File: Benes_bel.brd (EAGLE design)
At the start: 91.1 x 58.4 mm, 19 parts, among them J1 DCJ0202, K1 HE751, K2 HE751, K3 HE751, K4 HE751, T1 BC337, T2 BC337, T3 BC337, T4 BC337, X5 FH12-08S-1SH

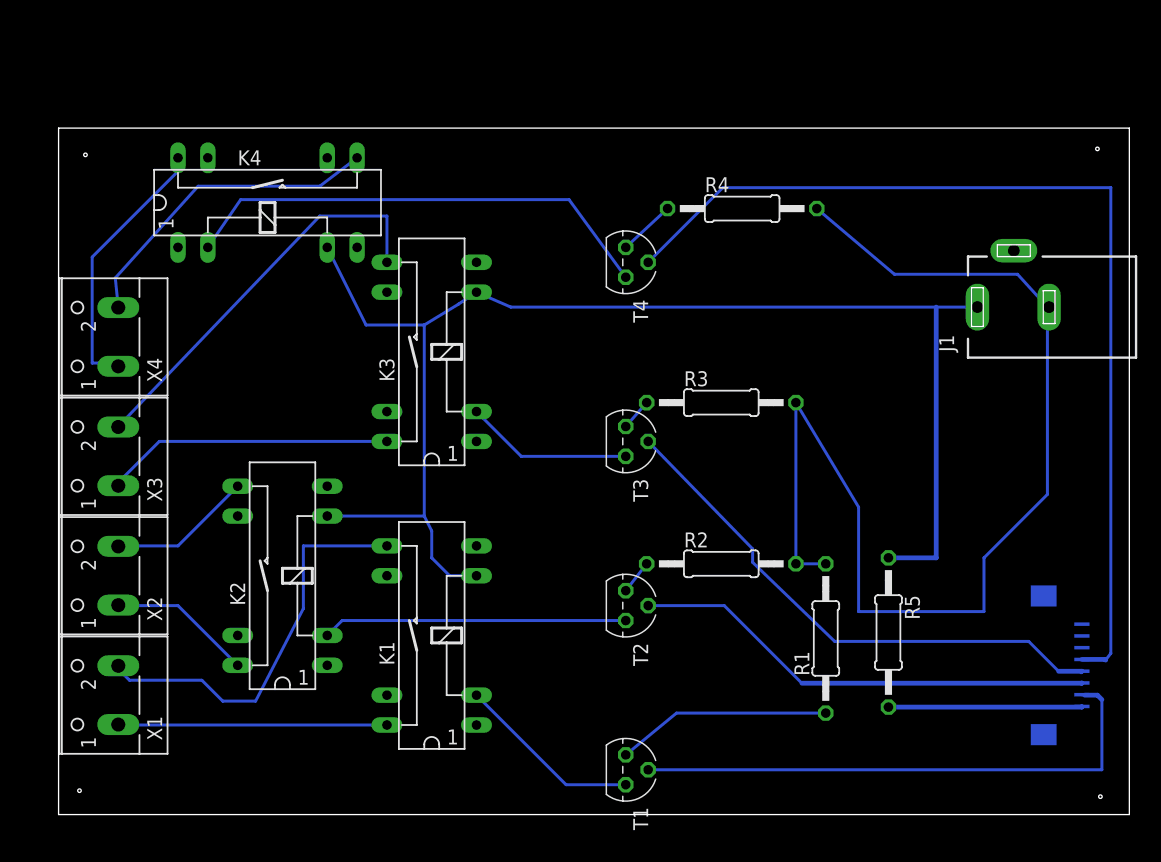
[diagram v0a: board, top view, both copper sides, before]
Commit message: Aanpassing van Benes_bel
dikkere lijnen, groter afstand voor frezen
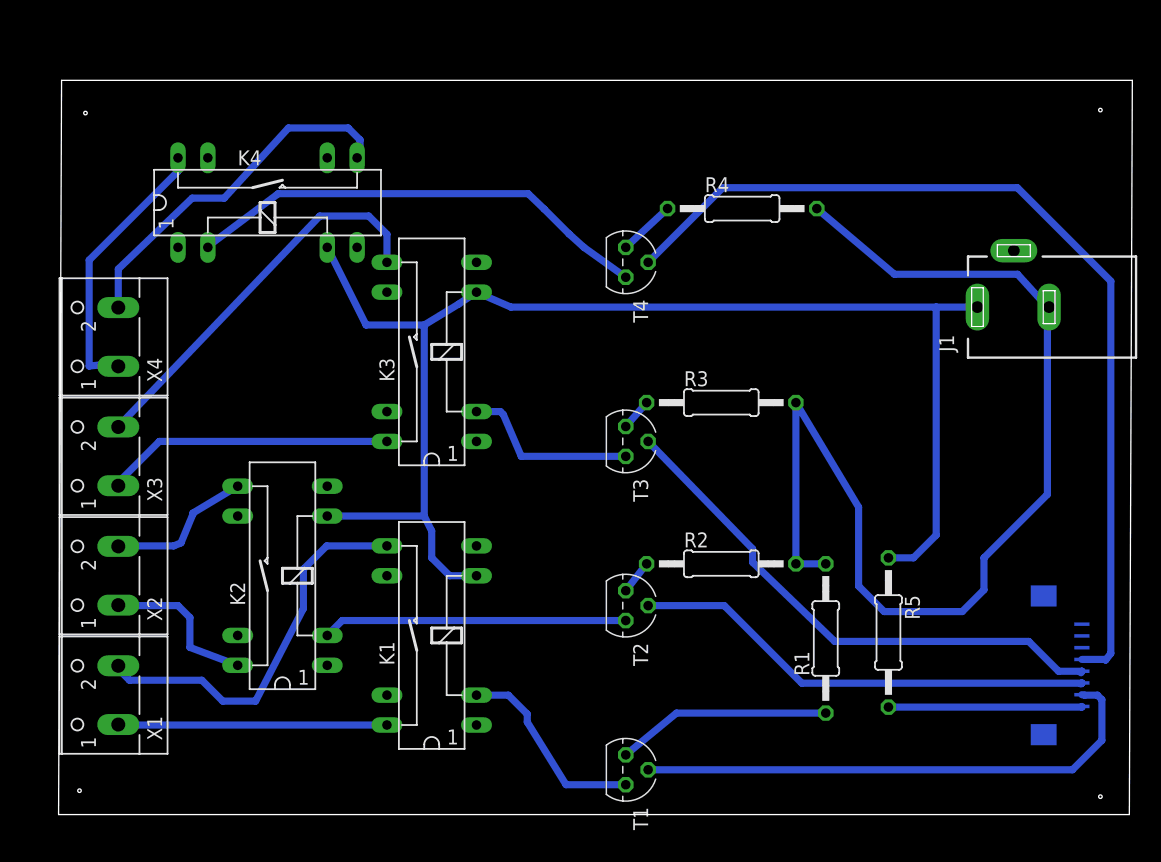
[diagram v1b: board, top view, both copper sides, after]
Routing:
- net N$10: track 84.4 -> 79.8 mm
- net N$18: track 27.4 -> 31.0 mm
- net N$6: track 97.4 -> 95.0 mm
- net N$7: track 46.4 -> 45.0 mm
- net N$20: track 41.1 -> 39.8 mm
- net N$12: track 34.4 -> 33.2 mm
- net N$23: track 15.9 -> 17.0 mm
- net N$21: track 118.5 -> 117.4 mm
- net N$13: track 12.3 -> 13.4 mm
- net N$16: track 34.5 -> 33.6 mm
- net N$19: track 14.3 -> 15.2 mm
- net N$17: track 23.0 -> 23.6 mm
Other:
- board size 91.1 x 58.4 mm -> 91.4 x 62.5 mm

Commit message: aanpassing met extra leds als controle tracks op 2 lagen Gerber files
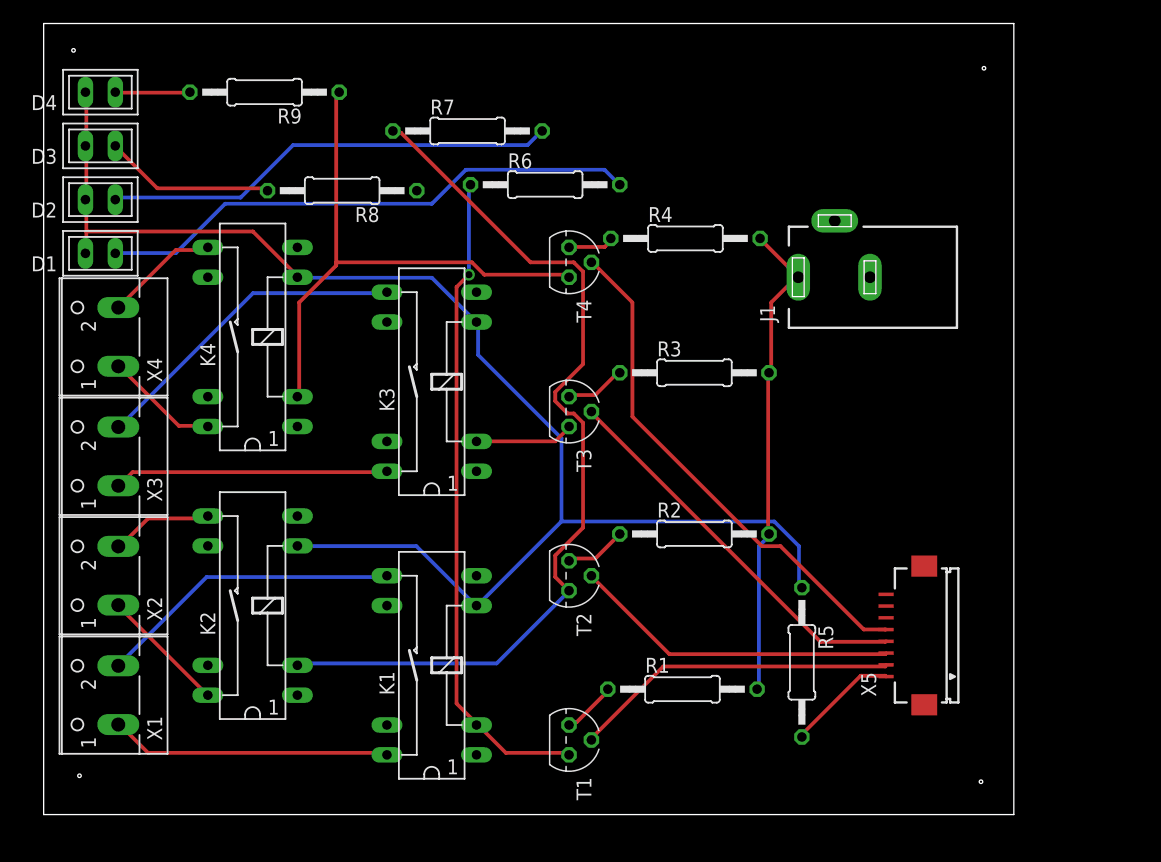
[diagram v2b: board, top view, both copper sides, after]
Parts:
- added D1, D2, D3, D4: U57X32, led:U57X32
- added R6, R7, R8, R9: 330k, resistor:0207/12
- moved J1 15.5 mm to (66.0, 45.7)
- moved R1 12.9 mm to (53.1, 10.7), turned to 0 degrees
- moved K4 11.5 mm to (16.5, 40.6), turned to 90 degrees
- moved X5 10.5 mm to (73.7, 15.2), flipped to the top
- moved R5 7.79 mm to (63.2, 13.0)
- moved T1 5.45 mm to (43.4, 6.35)
- moved T2 5.45 mm to (43.4, 20.3)
- moved T3 5.45 mm to (43.4, 34.3)
- moved R4 5.45 mm to (53.3, 49.0)
- moved T4 4.83 mm to (43.4, 47.0)
- moved K2 3.59 mm to (16.5, 17.8)
- moved R2 3.42 mm to (54.1, 23.9)
- moved R3 3.42 mm to (54.1, 37.6)
- moved K1 2.54 mm to (31.8, 12.7)
- moved K3 2.54 mm to (31.8, 36.8)
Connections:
- removed net N$21: J1.1, K1.6, K2.6, K3.6, K4.6, R5.1
- new net N$24: D4.A, R9.2
- new net N$25: D1.A, R6.2
- new net N$26: D2.A, R7.2
- new net N$27: D3.A, R8.2
- new net N$28: D1.K, D2.K, D3.K, D4.K, K1.6, K2.6, K3.6, K4.6, R5.1
- new net N$30: R8.1
- net N$20: now also R9.1
- net N$23: now also R6.1
- net N$5: now also R7.1
- net N$6: now also J1.1; no longer J1.3
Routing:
- net N$28: track 0.00 -> 122.6 mm
- net N$21: track 117.4 -> 0.00 mm
- net N$6: track 95.0 -> 41.3 mm
- net N$5: track 25.9 -> 77.8 mm
- net N$25: track 0.00 -> 46.4 mm
- net N$23: track 17.0 -> 56.1 mm, vias 0 -> 1
- net N$26: track 0.00 -> 38.7 mm
- net N$10: track 79.8 -> 43.7 mm
- net N$18: track 31.0 -> 9.79 mm
- net N$7: track 45.0 -> 27.8 mm
- net N$27: track 0.00 -> 14.5 mm
- net N$17: track 23.6 -> 9.72 mm
- net N$1: track 18.3 -> 4.70 mm
- net N$9: track 45.8 -> 33.2 mm
- net N$8: track 39.8 -> 27.9 mm
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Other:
- board size 91.4 x 62.5 mm -> 82.5 x 67.3 mm

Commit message: Bord werkt op eerste pcb ontbreken 3 draden in de schema's en de prod files is dit aangepast.
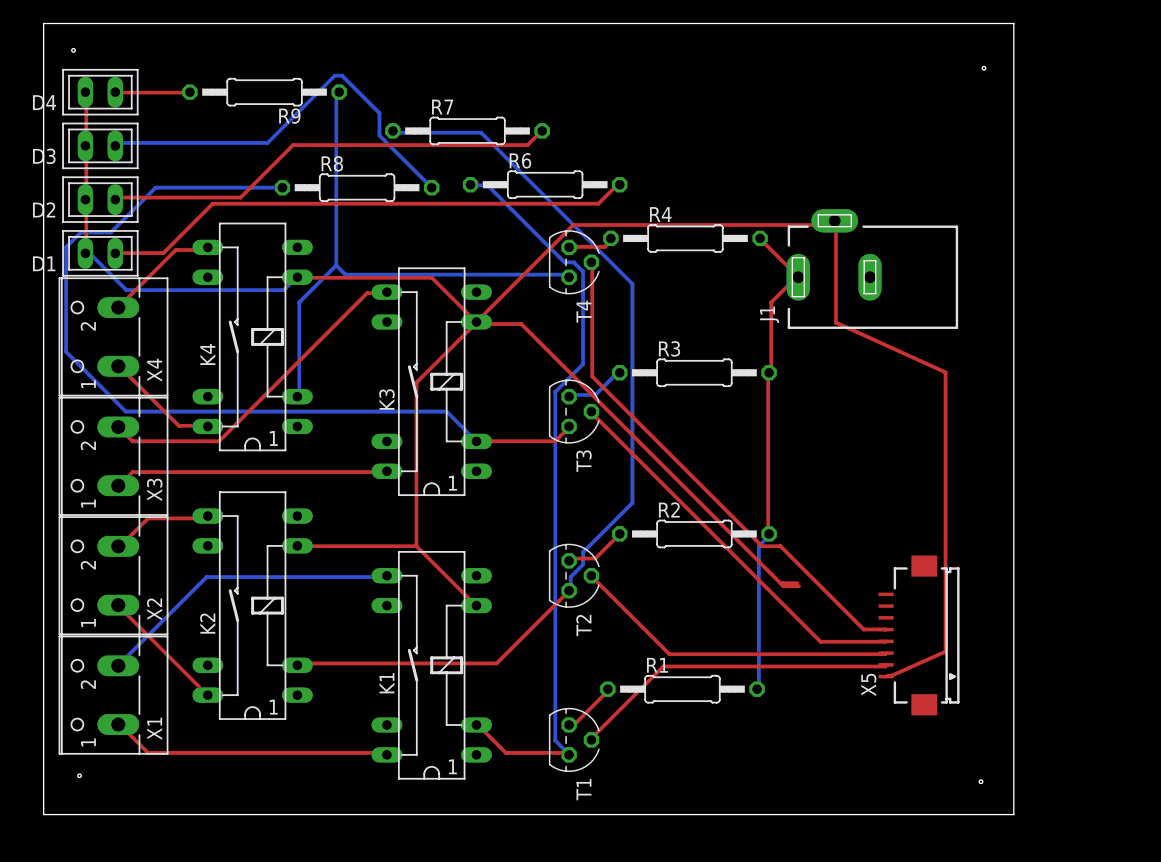
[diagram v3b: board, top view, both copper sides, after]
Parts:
- removed R5: (no value), resistor:0207/12
- moved R8 1.30 mm to (25.4, 53.3), turned to 0 degrees
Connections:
- removed net N$22: R5.2, X5.1
- removed net N$28: D1.K, D2.K, D3.K, D4.K, K1.6, K2.6, K3.6, K4.6, R5.1
- removed net N$30: R8.1
- new net N$21: D1.K, D2.K, D3.K, D4.K, J1.2, K1.6, K2.6, K3.6, K4.6, X5.1
- net N$19: now also R8.1
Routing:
- net N$21: track 0.00 -> 209.6 mm
- net N$28: track 122.6 -> 0.00 mm
- net N$19: track 8.43 -> 75.9 mm
- net N$27: track 14.5 -> 34.5 mm
- net N$22: track 9.47 -> 0.00 mm
- net N$23: track 56.1 -> 64.1 mm, vias 1 -> 0
- net N$5: track 77.8 -> 79.9 mm
- net N$25: track 46.4 -> 45.3 mm
- net N$16: track 27.6 -> 28.6 mm
- net N$6: track 41.3 -> 42.0 mm

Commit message: correctie bord: groter gaten vr DC Jack toevoeging van vcc naar display leds meer ruimte
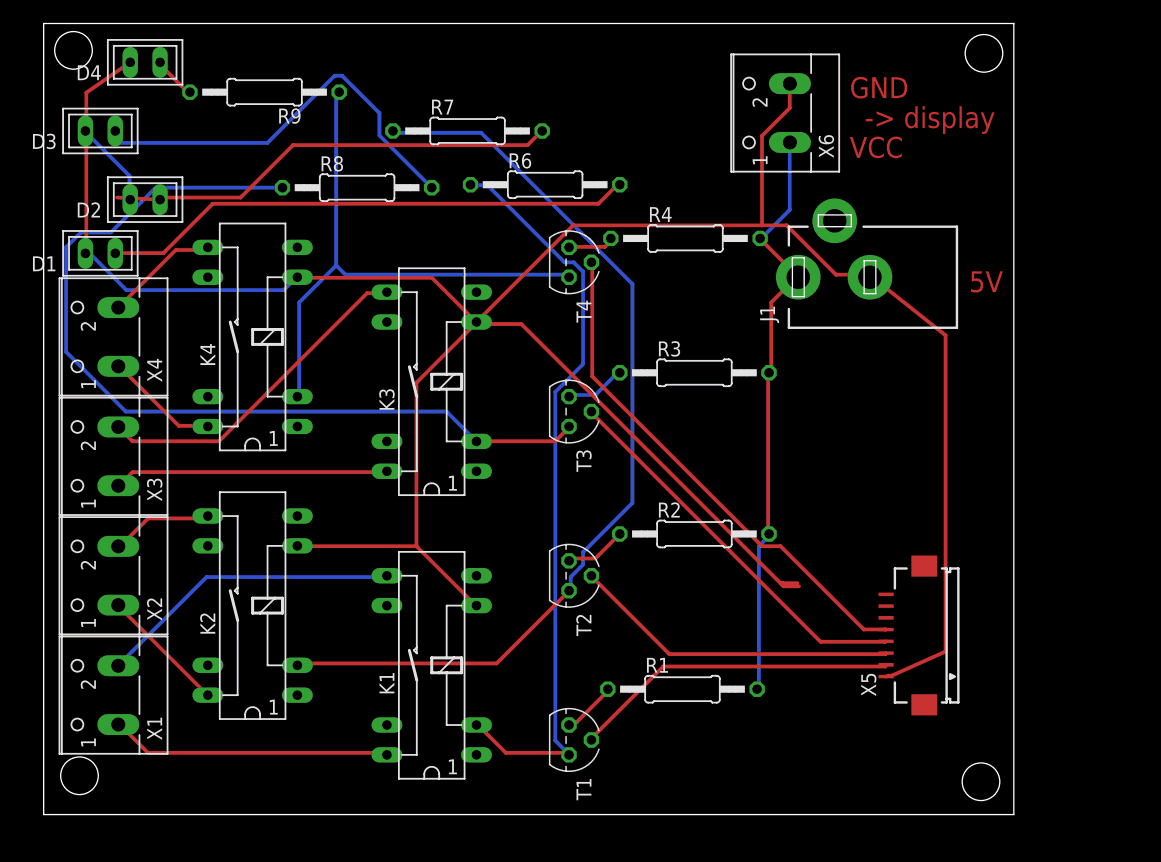
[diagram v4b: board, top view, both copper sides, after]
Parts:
- added X6: (no value), con-wago-500:W237-102
- moved D4 4.58 mm to (7.37, 64.0)
- moved D2 3.81 mm to (7.37, 52.3)
- moved D3 1.27 mm to (3.56, 58.2)
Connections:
- net N$21: now also J1.3, X6.2; no longer J1.2
- net N$6: now also X6.1
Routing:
- net N$21: track 209.6 -> 233.8 mm
- net N$6: track 42.0 -> 51.2 mm
- net N$24: track 6.36 -> 3.72 mm
- net N$27: track 34.5 -> 35.1 mm
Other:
- board text added: "-> display"
- board text added: "5V"
- board text added: "GND"
- board text added: "VCC"
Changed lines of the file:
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@@
 <board>
 <plain>
-<hole x="1.27" y="65.024" drill="0.3"/>
-<hole x="1.778" y="3.302" drill="0.3"/>
-<hole x="78.74" y="63.5" drill="0.3"/>
-<hole x="78.486" y="2.794" drill="0.3"/>
+<hole x="1.27" y="65.024" drill="3.2"/>
+<hole x="1.778" y="3.302" drill="3.2"/>
+<hole x="78.74" y="64.77" drill="3.2"/>
+<hole x="78.486" y="2.794" drill="3.2"/>
 <wire x1="-1.27" y1="0" x2="-1.27" y2="67.31" width="0" layer="20"/>
 <wire x1="-1.27" y1="67.31" x2="81.28" y2="67.31" width="0" layer="20"/>
 <wire x1="81.28" y1="67.31" x2="81.28" y2="0" width="0" layer="20"/>
 <wire x1="81.28" y1="0" x2="-1.27" y2="0" width="0" layer="20"/>
+<text x="67.31" y="55.88" size="1.778" layer="1">VCC</text>
+<text x="67.31" y="60.96" size="1.778" layer="1">GND</text>
+<text x="68.58" y="58.42" size="1.778" layer="1">-&gt; display</text>
+<text x="77.47" y="44.45" size="1.778" layer="1">5V</text>
 </plain>
 <attributes>
@@
 <element name="R9" library="resistor" package="0207/12" value="330k" x="17.526" y="61.468" rot="R180"/>
 <element name="D1" library="led" package="U57X32" value="U57X32" x="3.556" y="47.752" rot="R180"/>
-<element name="D2" library="led" package="U57X32" value="U57X32" x="3.556" y="52.324" rot="R180"/>
-<element name="D3" library="led" package="U57X32" value="U57X32" x="3.556" y="56.896" rot="R180"/>
-<element name="D4" library="led" package="U57X32" value="U57X32" x="3.556" y="61.468" rot="R180"/>
+<element name="D2" library="led" package="U57X32" value="U57X32" x="7.366" y="52.324" rot="R180"/>
+<element name="D3" library="led" package="U57X32" value="U57X32" x="3.556" y="58.166" rot="R180"/>
+<element name="D4" library="led" package="U57X32" value="U57X32" x="7.366" y="64.008" rot="R180"/>
 <element name="R8" library="resistor" package="0207/12" value="330k" x="25.4" y="53.34"/>
+<element name="X6" library="con-wago-500" package="W237-102" value="" x="60.96" y="59.69" rot="R90">
+<attribute name="OC_FARNELL" value="unknown" x="60.96" y="59.69" size="1.778" layer="27" rot="R90" display="off"/>
+<attribute name="OC_NEWARK" value="70K9898" x="60.96" y="59.69" size="1.778" layer="27" rot="R90" display="off"/>
+<attribute name="MPN" value="237-102" x="60.96" y="59.69" size="1.778" layer="27" rot="R90" display="off"/>
+<attribute name="MF" value="" x="60.96" y="59.69" size="1.778" layer="27" rot="R90" display="off"/>
+</element>
 </elements>
 <signals>
@@
 <wire x1="62.865" y1="45.72" x2="62.94" y2="45.72" width="0.32" layer="1"/>
 <wire x1="62.865" y1="45.72" x2="62.7375" y2="45.675" width="0.32" layer="1"/>
+<contactref element="X6" pad="1"/>
+<wire x1="62.2125" y1="51.45" x2="62.2125" y2="56.9625" width="0.32" layer="16"/>
+<wire x1="59.85" y1="49.0875" x2="62.2125" y2="51.45" width="0.32" layer="16"/>
+<wire x1="62.2125" y1="56.9625" x2="62.23" y2="57.19" width="0.32" layer="16"/>
+<wire x1="59.85" y1="49.0875" x2="59.69" y2="49.022" width="0.32" layer="16"/>
 </signal>
 <signal name="N$7">
@@
 <contactref element="D2" pad="A"/>
 <contactref element="R7" pad="2"/>
-<wire x1="15.4875" y1="52.5" x2="4.9875" y2="52.5" width="0.32" layer="1"/>
 <wire x1="19.95" y1="56.9625" x2="15.4875" y2="52.5" width="0.32" layer="1"/>
 <wire x1="39.9" y1="56.9625" x2="19.95" y2="56.9625" width="0.32" layer="1"/>
 <wire x1="40.95" y1="58.0125" x2="39.9" y2="56.9625" width="0.32" layer="1"/>
-<wire x1="4.9875" y1="52.5" x2="4.826" y2="52.324" width="0.32" layer="1"/>
+<wire x1="4.9875" y1="52.5" x2="8.636" y2="52.324" width="0.32" layer="1"/>
 <wire x1="40.95" y1="58.0125" x2="41.148" y2="58.166" width="0.32" layer="1"/>
+<wire x1="15.4875" y1="52.5" x2="8.6625" y2="52.5" width="0.32" layer="1"/>
+<wire x1="8.6625" y1="52.5" x2="8.636" y2="52.324" width="0.32" layer="1"/>
 </signal>
 <signal name="N$24">
 <contactref element="D4" pad="A"/>
 <contactref element="R9" pad="2"/>
-<wire x1="11.025" y1="61.425" x2="4.9875" y2="61.425" width="0.32" layer="1"/>
-<wire x1="4.9875" y1="61.425" x2="4.826" y2="61.468" width="0.32" layer="1"/>
+<wire x1="11.025" y1="61.425" x2="8.6625" y2="63.7875" width="0.32" layer="1"/>
+<wire x1="8.6625" y1="63.7875" x2="8.636" y2="64.008" width="0.32" layer="1"/>
 <wire x1="11.025" y1="61.425" x2="11.176" y2="61.468" width="0.32" layer="1"/>
 </signal>
@@
 <wire x1="20.475" y1="22.8375" x2="20.32" y2="22.86" width="0.32" layer="1"/>
 <wire x1="35.4375" y1="17.85" x2="35.56" y2="17.78" width="0.32" layer="1"/>
-<wire x1="2.3625" y1="52.2375" x2="2.3625" y2="47.775" width="0.32" layer="1"/>
 <wire x1="2.3625" y1="47.775" x2="2.286" y2="47.752" width="0.32" layer="1"/>
-<wire x1="2.3625" y1="52.2375" x2="2.286" y2="52.324" width="0.32" layer="1"/>
-<wire x1="2.3625" y1="52.5" x2="2.3625" y2="56.7" width="0.32" layer="1"/>
-<wire x1="2.3625" y1="56.7" x2="2.286" y2="56.896" width="0.32" layer="1"/>
-<wire x1="2.3625" y1="52.5" x2="2.286" y2="52.324" width="0.32" layer="1"/>
+<wire x1="2.3625" y1="47.775" x2="2.3625" y2="56.7" width="0.32" layer="1"/>
+<wire x1="2.3625" y1="56.7" x2="2.286" y2="58.166" width="0.32" layer="1"/>
 <wire x1="2.3625" y1="56.9625" x2="2.3625" y2="61.425" width="0.32" layer="1"/>
-<wire x1="2.3625" y1="61.425" x2="2.286" y2="61.468" width="0.32" layer="1"/>
-<wire x1="2.3625" y1="56.9625" x2="2.286" y2="56.896" width="0.32" layer="1"/>
+<wire x1="2.3625" y1="61.425" x2="6.096" y2="64.008" width="0.32" layer="1"/>
+<wire x1="2.3625" y1="56.9625" x2="2.286" y2="58.166" width="0.32" layer="1"/>
 <wire x1="31.7625" y1="45.675" x2="20.475" y2="45.675" width="0.32" layer="1"/>
 <wire x1="35.4375" y1="42" x2="31.7625" y2="45.675" width="0.32" layer="1"/>
@@
 <wire x1="35.4375" y1="41.7375" x2="30.45" y2="36.75" width="0.32" layer="1"/>
 <wire x1="35.4375" y1="41.7375" x2="35.56" y2="41.91" width="0.32" layer="1"/>
-<contactref element="J1" pad="2"/>
 <wire x1="61.595" y1="19.685" x2="62.865" y2="19.685" width="0.32" layer="1"/>
 <wire x1="61.595" y1="19.685" x2="61.51125" y2="19.60125" width="0.32" layer="1"/>
-<wire x1="43.815" y1="50.165" x2="35.56" y2="41.91" width="0.32" layer="1"/>
-<wire x1="66.04" y1="50.165" x2="43.815" y2="50.165" width="0.32" layer="1"/>
-<wire x1="66.04" y1="50.165" x2="66.04" y2="50.52" width="0.32" layer="1"/>
+<wire x1="43.815" y1="50.165" x2="43.8125" y2="50.1625" width="0.32" layer="1"/>
 <contactref element="X5" pad="1"/>
+<contactref element="J1" pad="3"/>
+<wire x1="43.8125" y1="50.1625" x2="35.56" y2="41.91" width="0.32" layer="1"/>
 <wire x1="70.875" y1="11.8125" x2="70.6125" y2="11.8125" width="0.32" layer="1"/>
 <wire x1="75.4725" y1="13.87" x2="70.875" y2="11.8125" width="0.32" layer="1"/>
-<wire x1="75.4725" y1="37.6225" x2="75.4725" y2="13.87" width="0.32" layer="1"/>
-<wire x1="66.15" y1="41.865" x2="75.4725" y2="37.6225" width="0.32" layer="1"/>
-<wire x1="66.15" y1="50.1375" x2="66.15" y2="41.865" width="0.32" layer="1"/>
+<wire x1="75.4725" y1="40.7725" x2="75.4725" y2="13.87" width="0.32" layer="1"/>
+<wire x1="69.3" y1="45.675" x2="75.4725" y2="40.7725" width="0.32" layer="1"/>
 <wire x1="70.6125" y1="11.8125" x2="70.41" y2="11.74" width="0.32" layer="1"/>
-<wire x1="66.15" y1="50.1375" x2="66.04" y2="50.52" width="0.32" layer="1"/>
+<wire x1="43.8375" y1="50.1375" x2="43.8125" y2="50.1625" width="0.32" layer="1"/>
+<wire x1="69.3" y1="45.675" x2="69.04" y2="45.72" width="0.32" layer="1"/>
+<wire x1="66.15" y1="45.9375" x2="69.0375" y2="45.9375" width="0.32" layer="1"/>
+<wire x1="61.95" y1="50.1375" x2="66.15" y2="45.9375" width="0.32" layer="1"/>
+<wire x1="43.8375" y1="50.1375" x2="59.85" y2="50.1375" width="0.32" layer="1"/>
+<wire x1="59.85" y1="50.1375" x2="61.95" y2="50.1375" width="0.32" layer="1"/>
+<wire x1="69.0375" y1="45.9375" x2="69.04" y2="45.72" width="0.32" layer="1"/>
+<contactref element="X6" pad="2"/>
+<wire x1="62.2125" y1="60.1125" x2="62.2125" y2="61.95" width="0.32" layer="1"/>
+<wire x1="59.85" y1="57.75" x2="62.2125" y2="60.1125" width="0.32" layer="1"/>
+<wire x1="59.85" y1="50.1375" x2="59.85" y2="57.75" width="0.32" layer="1"/>
+<wire x1="62.2125" y1="61.95" x2="62.23" y2="62.19" width="0.32" layer="1"/>
+<wire x1="6.0375" y1="54.3375" x2="6.0375" y2="52.5" width="0.32" layer="16"/>
+<wire x1="2.3625" y1="58.0125" x2="6.0375" y2="54.3375" width="0.32" layer="16"/>
+<wire x1="6.0375" y1="52.5" x2="6.096" y2="52.324" width="0.32" layer="16"/>
+<wire x1="2.3625" y1="58.0125" x2="2.286" y2="58.166" width="0.32" layer="16"/>
 </signal>
 <signal name="N$27">
@@
 <wire x1="27.305" y1="57.785" x2="27.305" y2="59.69" width="0.32" layer="16"/>
 <wire x1="31.75" y1="53.34" x2="27.305" y2="57.785" width="0.32" layer="16"/>
-<wire x1="5.08" y1="57.15" x2="4.826" y2="56.896" width="0.32" layer="16"/>
+<wire x1="5.08" y1="57.15" x2="4.826" y2="58.166" width="0.32" layer="16"/>
 </signal>
 </signals>
